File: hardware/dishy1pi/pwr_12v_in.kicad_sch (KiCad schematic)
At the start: 5 parts, among them SW2 SS-12F49-G050, U13 TPS561201DDCR, U14 CYA0630-10UH

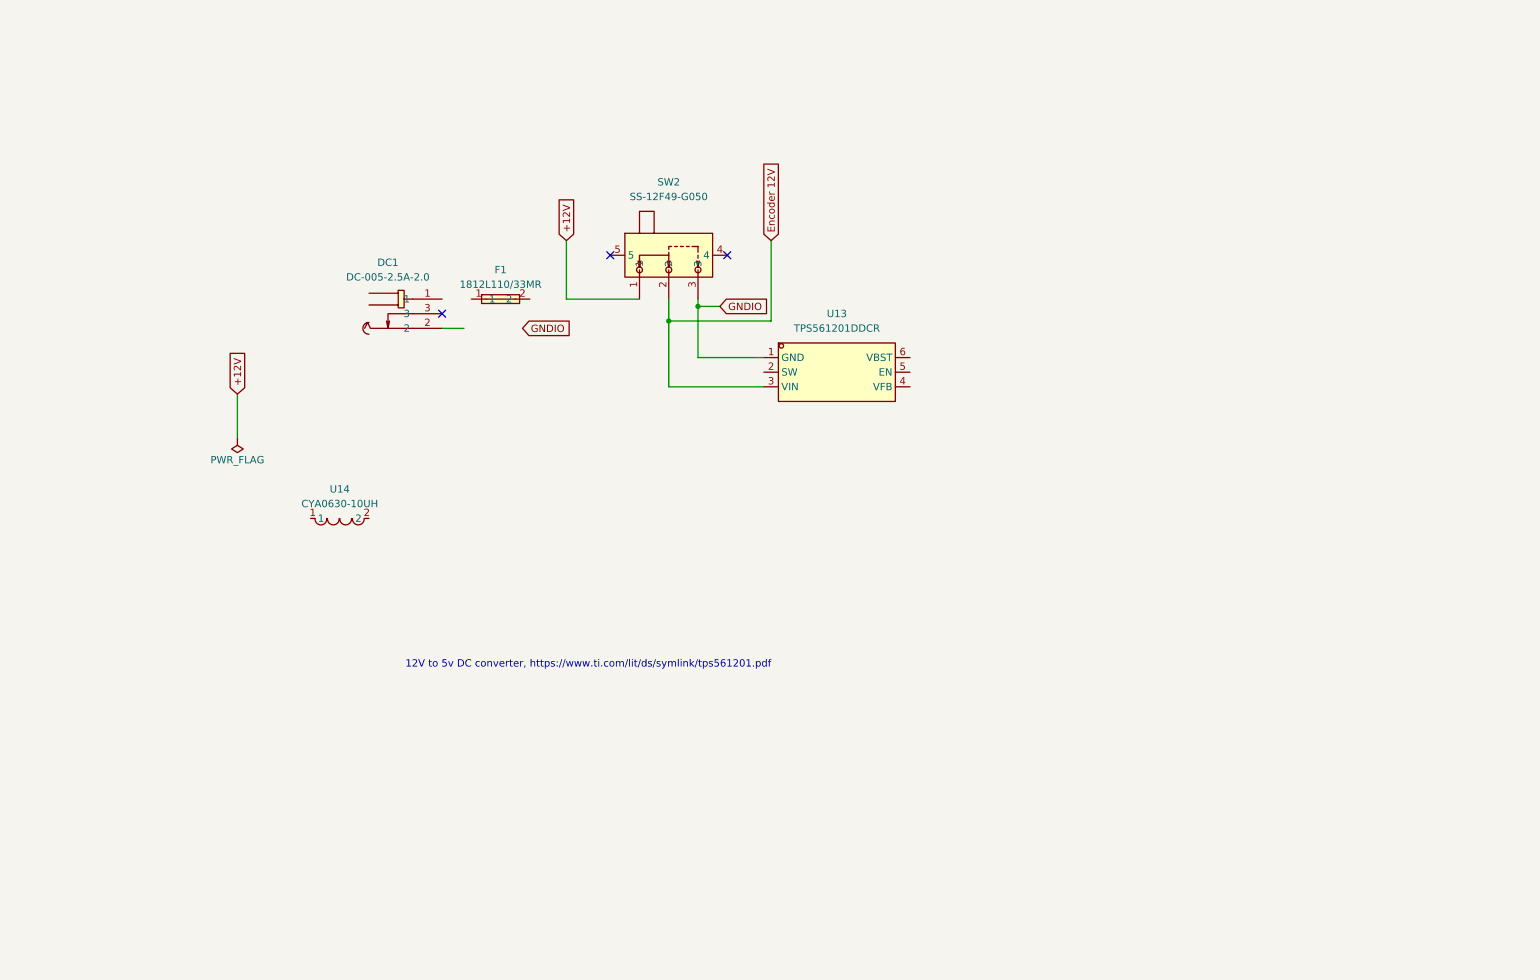
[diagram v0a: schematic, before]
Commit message: Added power circuit to dishy schematic
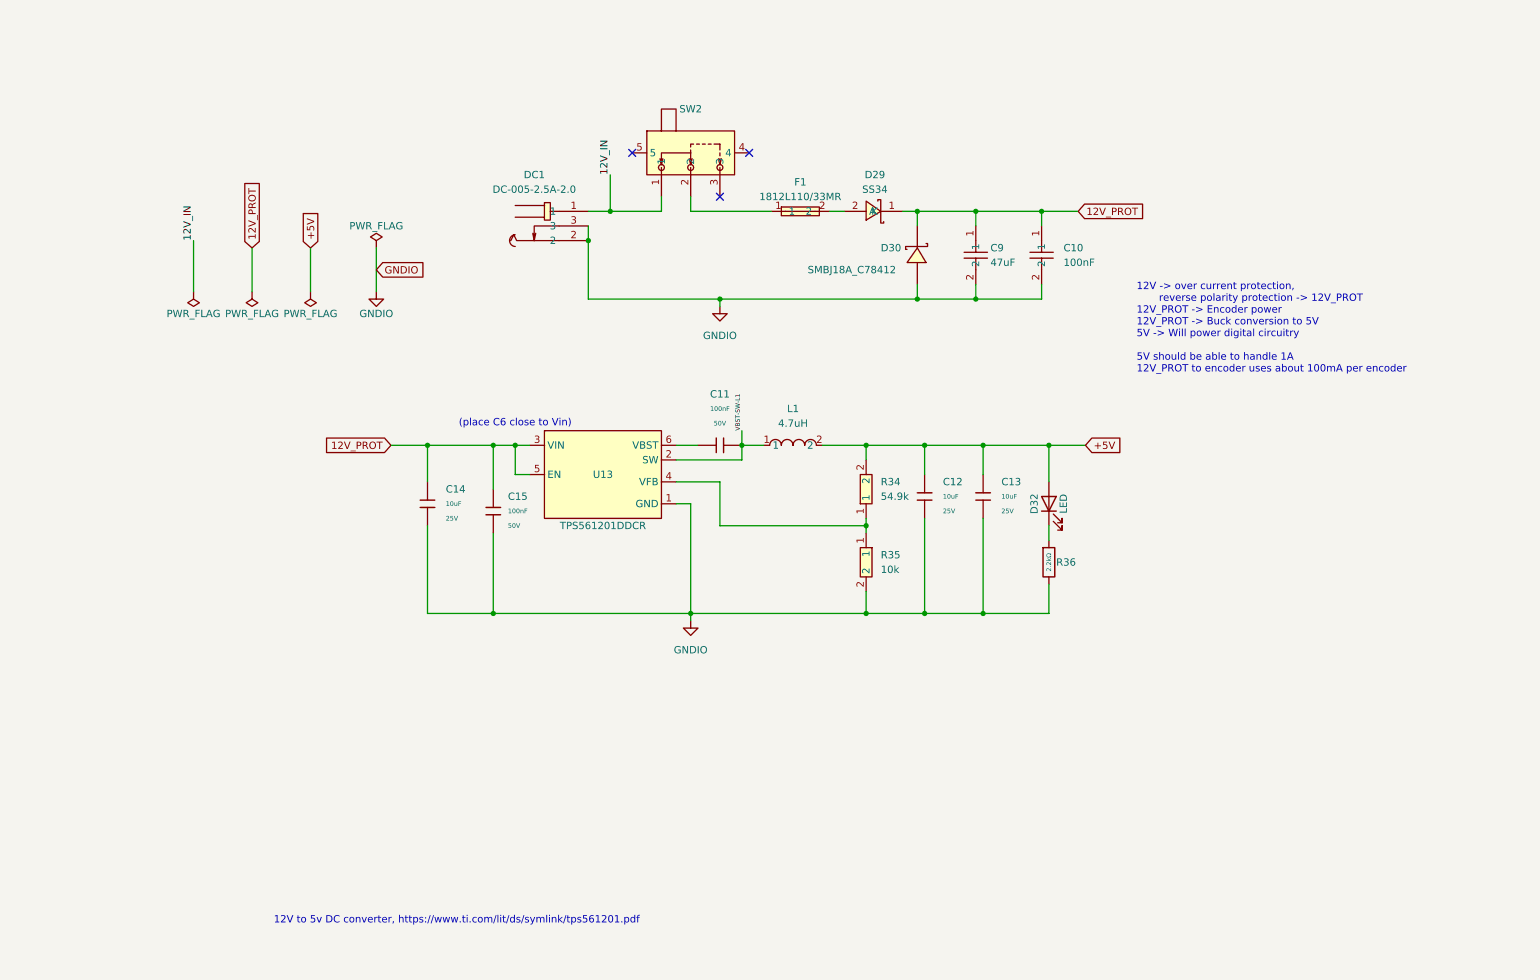
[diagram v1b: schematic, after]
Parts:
- removed DC1: DC-005-2.5A-2.0, MyParts:CONN-TH_DC-005-2.5A-2.0, symbol MyParts:DC-005-2.5A-2.0
- removed F1: 1812L110/33MR, MyParts:F1812, symbol MyParts:1812L110_33MR
- removed SW2: SS-12F49-G050, MyParts:SW-TH_SS-12F45-GXXX, symbol MyParts:SS-12F49-G050
- removed U13: TPS561201DDCR, MyParts:SOT-23-6_L2.9-W1.6-P0.95-LS2.8-BR, symbol MyParts:TPS561201DDCR
- removed U14: CYA0630-10UH, MyParts:IND-SMD_L7.2-W6.6_GPSR07X0, symbol MyParts:CYA0630-10UH
- added C10: 100nF, PowerSupply:C0603, symbol PowerSupply:CC0603KRX7R9BB104
- added C11: 100nF, PCM_JLCPCB:C_0402, symbol PCM_JLCPCB-Capacitors:0402,100nF,(2)
- added C12, C13, C14: 10uF, PCM_JLCPCB:C_0805, symbol PCM_JLCPCB-Capacitors:0805,10uF
- added C15: 100nF, PCM_JLCPCB:C_0805, symbol PCM_JLCPCB-Capacitors:0805,100nF,(2)
- added C9: 47uF, PowerSupply:C1206, symbol PowerSupply:GRM31CR61E476ME44L
- added D29: SS34, PowerSupply:SMA_L4.3-W2.6-LS5.2-RD, symbol PowerSupply:SS34_C8678
- added D30: SMBJ18A_C78412, MyParts:SMB_L4.6-W3.6-LS5.3-RD, symbol PowerSupply:SMBJ18A_C78412
- added D32: LED, LED_SMD:LED_1206_3216Metric, symbol Device:LED
- added DC1: DC-005-2.5A-2.0, PowerSupply:CONN-TH_DC-005-2.5A-2.0, symbol PowerSupply:DC-005-2.5A-2.0
- added F1: 1812L110/33MR, PowerSupply:F1812, symbol PowerSupply:1812L110_33MR
- added L1: 4.7uH, PowerSupply:IND-SMD_L3.0-W3.0-1, symbol PowerSupply:ANR3015T4R7M
- added R34: 54.9k, PowerSupply:R0603, symbol PowerSupply:0603WAF5492T5E
- added R35: 10k, PowerSupply:R0603, symbol PowerSupply:0603WAF1002T5E
- added R36: 2.2kΩ, PCM_JLCPCB:R_0402, symbol PCM_JLCPCB-Resistors:0402,2.2kΩ
- added SW2: SS-12F49-G050, PowerSupply:SW-TH_SS-12F45-GXXX, symbol PowerSupply:SS-12F49-G050
- added U13: TPS561201DDCR, PowerSupply:SOT-23-6_L2.9-W1.6-P0.95-LS2.8-BR, symbol PowerSupply:TPS561201DDCR
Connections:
- net GNDIO: now also C10.2, C12.2, C13.2, C14.2, C15.2, C9.2, D30.2 (A), DC1.2, DC1.3, R35.2, R36.2, U13.1 (GND)
- new net: R34.1, R35.1, U13.4 (VFB)
- new net: C11.1, U13.6 (VBST)
- new net: D32.1 (K), R36.1
- new net: D29.2 (A), F1.2
- new net: F1.1, SW2.2
- new net +5V: C12.1, C13.1, D32.2 (A), L1.2, R34.2
- new net 12V_IN: DC1.1, SW2.1
- new net 12V_PROT: C10.1, C14.1, C15.1, C9.1, D29.1 (K), D30.1 (K), U13.3 (VIN), U13.5 (EN)
- new net VBST-SW-L1: C11.2, L1.1, U13.2 (SW)
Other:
- note added: "(place C6 close to Vin)"
- note added: "12V -> over current protection, reverse polarity protection -> 12V_PROT 12V_PROT -> Encoder power 12V_PROT -> Buck conversion to 5V 5V -> Will power digital circuitry 5V should be able to handle 1A 12V_PROT to encoder uses about 100mA per encoder"

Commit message: Added 12V power input
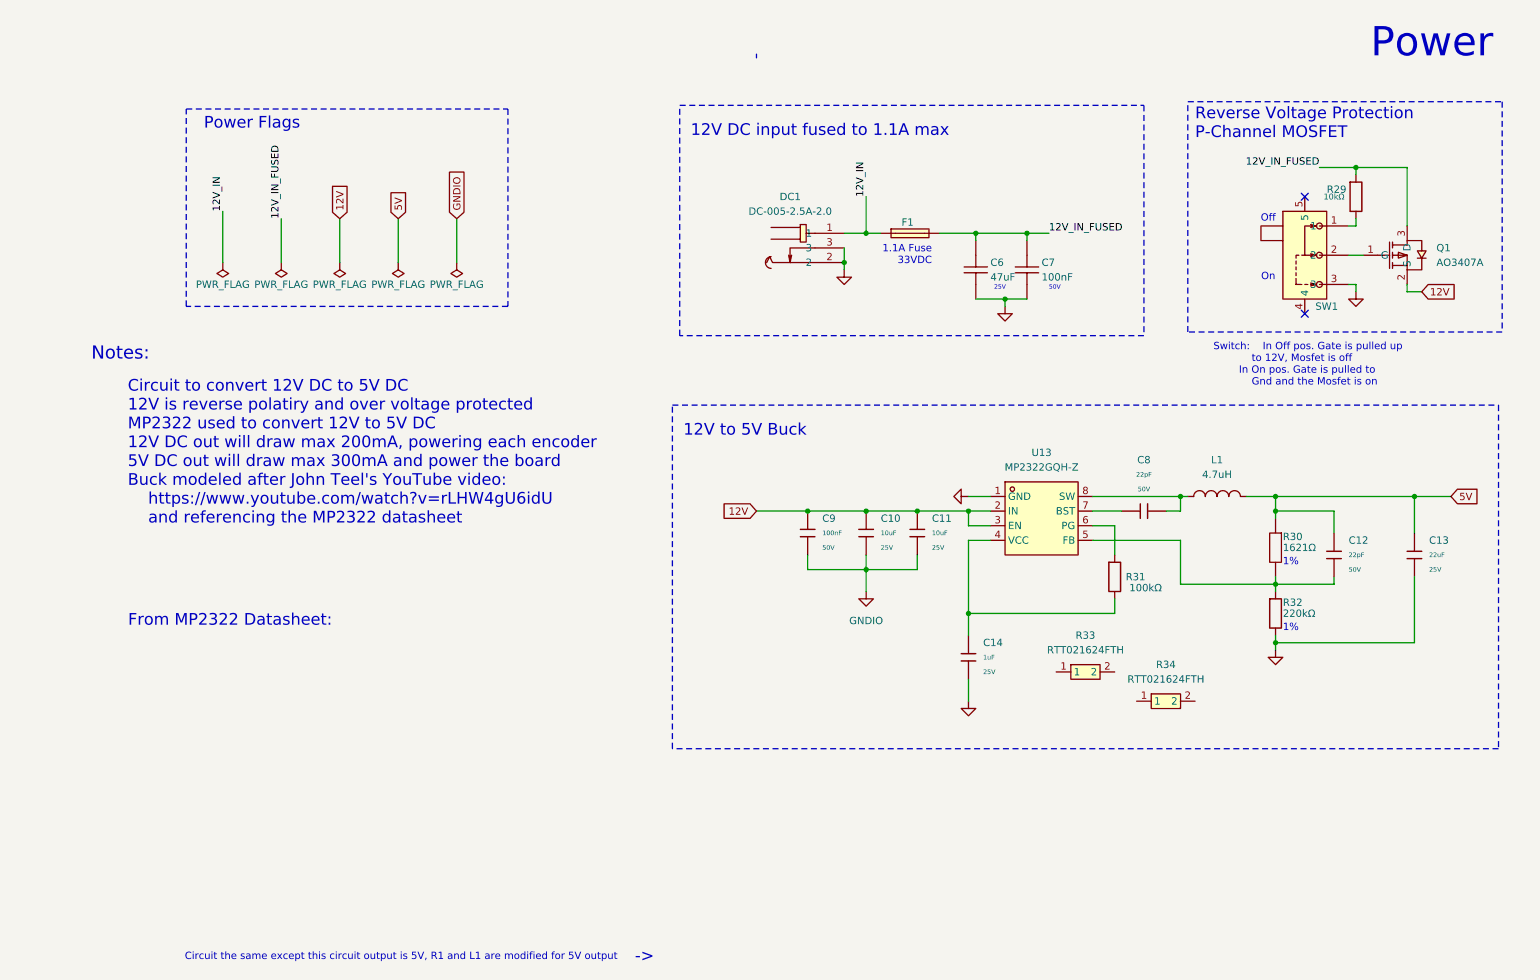
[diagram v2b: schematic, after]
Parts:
- removed C10: 100nF, PowerSupply:C0603, symbol PowerSupply:CC0603KRX7R9BB104
- removed C11: 100nF, PCM_JLCPCB:C_0402, symbol PCM_JLCPCB-Capacitors:0402,100nF,(2)
- removed C12, C13, C14: 10uF, PCM_JLCPCB:C_0805, symbol PCM_JLCPCB-Capacitors:0805,10uF
- removed C15: 100nF, PCM_JLCPCB:C_0805, symbol PCM_JLCPCB-Capacitors:0805,100nF,(2)
- removed C9: 47uF, PowerSupply:C1206, symbol PowerSupply:GRM31CR61E476ME44L
- removed D29: SS34, PowerSupply:SMA_L4.3-W2.6-LS5.2-RD, symbol PowerSupply:SS34_C8678
- removed D30: SMBJ18A_C78412, MyParts:SMB_L4.6-W3.6-LS5.3-RD, symbol PowerSupply:SMBJ18A_C78412
- removed D32: LED, LED_SMD:LED_1206_3216Metric, symbol Device:LED
- removed R34: 54.9k, PowerSupply:R0603, symbol PowerSupply:0603WAF5492T5E
- removed R35: 10k, PowerSupply:R0603, symbol PowerSupply:0603WAF1002T5E
- removed R36: 2.2kΩ, PCM_JLCPCB:R_0402, symbol PCM_JLCPCB-Resistors:0402,2.2kΩ
- removed SW2: SS-12F49-G050, PowerSupply:SW-TH_SS-12F45-GXXX, symbol PowerSupply:SS-12F49-G050
- removed U13: TPS561201DDCR, PowerSupply:SOT-23-6_L2.9-W1.6-P0.95-LS2.8-BR, symbol PowerSupply:TPS561201DDCR
- added C10, C11: 10uF, PCM_JLCPCB:C_0603, symbol PCM_JLCPCB-Capacitors:0603,10uF,(2)
- added C12: 22pF, PCM_JLCPCB:C_0603, symbol PCM_JLCPCB-Capacitors:0603,22pF
- added C13: 22uF, PCM_JLCPCB:C_0805, symbol PCM_JLCPCB-Capacitors:0805,22uF
- added C14: 1uF, PCM_JLCPCB:C_0402, symbol PCM_JLCPCB-Capacitors:0402,1uF
- added C6: 47uF, PowerSupply:C1206, symbol PowerSupply:GRM31CR61E476ME44L
- added C7: 100nF, PowerSupply:C0603, symbol PowerSupply:CC0603KRX7R9BB104
- added C8: 22pF, PCM_JLCPCB:C_0402, symbol PCM_JLCPCB-Capacitors:0402,22pF
- added C9: 100nF, PCM_JLCPCB:C_0603, symbol PCM_JLCPCB-Capacitors:0603,100nF
- added Q1: AO3407A, PowerSupply:SOT-23-3_L2.9-W1.6-P1.90-LS2.8-BR, symbol PowerSupply:AO3407A
- added R29: 10kΩ, PCM_JLCPCB:R_0603, symbol PCM_JLCPCB-Resistors:0603,10kΩ
- added R30: 1621Ω, PowerSupply:R0603, symbol PowerSupply:0603WAF1621T5E
- added R31: 100kΩ, PCM_JLCPCB:R_0603, symbol PCM_JLCPCB-Resistors:0603,100kΩ
- added R32: 220kΩ, PCM_JLCPCB:R_0603, symbol PCM_JLCPCB-Resistors:0603,220kΩ
- added R33, R34: RTT021624FTH, myparts:R0402, symbol MyParts:RTT021624FTH
- added SW1: SS-12F49-G050, PowerSupply:SW-TH_SS-12F45-GXXX, symbol PowerSupply:SS-12F49-G050
- added U13: MP2322GQH-Z, PowerSupply:QFN-8_L2.0-W1.5-P0.50-BL, symbol PowerSupply:MP2322GQH-Z
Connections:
- net 12V_IN: now also F1.1
- net GNDIO: now also C10.2, C11.2, C13.2, C14.2, C6.2, C7.2, C9.2, R32.2, SW1.3, U13.1 (GND)
- net 12V_IN_FUSED: now reaches F1.2
- net 12V_IN_FUSED: now also C6.1, C7.1, Q1.3 (D), R29.1
- net +5V renamed 5V
- net 5V: now also C12.1, C13.1, R30.1
- net VBST-SW-L1: no longer names the net of L1.1
- net VBST-SW-L1: now also C8.2, U13.8 (SW)
- new net: Q1.1 (G), SW1.2
- new net: C12.2, R30.2, R32.1, U13.5 (FB)
- new net: R31.1, U13.6 (PG)
- new net: C14.1, R31.2, U13.4 (VCC)
- new net: C8.1, U13.7 (BST)
- new net: R29.2, SW1.1
- new net 12V: C10.1, C11.1, C9.1, Q1.2 (S), U13.2 (IN), U13.3 (EN)
- no-connect marks 3 -> 2
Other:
- note added: "->"
- note added: "1%"
- note added: "1.1A Fuse 33VDC"
- note added: "12V DC input fused to 1.1A max"
- note added: "12V to 5V Buck"
- note added: "25V"
- note added: "50V"
- note added: "Circuit the same except this circuit output is 5V, R1 and L1 are modified for 5V output"
- note added: "Circuit to convert 12V DC to 5V DC 12V is reverse polatiry and over voltage protected MP2322 used to convert 12V to 5V DC 12V DC out will draw max 200mA, powering each encoder 5V DC out will draw max 300mA and power the board Buck modeled after John Teel's YouTube video: https://www.youtube.com/watch?v=rLHW4gU6idU and referencing the MP2322 datasheet"
- note added: "From MP2322 Datasheet:"
- note added: "Notes:"
- note added: "Off"
- note added: "On"
- note added: "Power"
- note added: "Power Flags"
- note added: "Reverse Voltage Protection P-Channel MOSFET"
- note added: "Switch: In Off pos. Gate is pulled up to 12V, Mosfet is off In On pos. Gate is pulled to Gnd and the Mosfet is on"
- note removed: "(place C6 close to Vin)"
- note removed: "12V -> over current protection, reverse polarity protection -> 12V_PROT 12V_PROT -> Encoder power 12V_PROT -> Buck conversion to 5V 5V -> Will power digital circuitry 5V should be able to handle 1A 12V_PROT to encoder uses about 100mA per encoder"
- note removed: "12V to 5v DC converter, https://www.ti.com/lit/ds/symlink/tps561201.pdf"
- company: (none) -> JRDish
- moved on the sheet: DC1

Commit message: Little change
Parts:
- removed R30: 1621Ω, PowerSupply:R0603, symbol PowerSupply:0603WAF1621T5E
- removed R33, R34: RTT021624FTH, myparts:R0402, symbol MyParts:RTT021624FTH
- added R30: 1624k, MyParts:R0603, symbol MyParts:RS-03L1624FT
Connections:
- net at R32.1, U13.5 (FB): now also R30.1; no longer C12.2
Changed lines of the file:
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@@
 	(text "1%"
 		(exclude_from_sim no)
-		(at 224.79 113.03 0)
+		(at 224.79 114.3 0)
 		(effects
 			(font
@@
 	)
 	(junction
+		(at 223.52 115.57)
+		(diameter 0)
+		(color 0 0 0 0)
+	)
+	(junction
 		(at 223.52 104.14)
 		(diameter 0)
@@
 	(wire
 		(pts
-			(xy 233.68 116.84) (xy 223.52 116.84)
+			(xy 232.41 115.57) (xy 223.52 115.57)
 		)
 		(stroke
@@
 	(wire
 		(pts
+			(xy 223.52 115.57) (xy 222.25 115.57)
+		)
+		(stroke
+			(width 0)
+			(type default)
+		)
+	)
+	(wire
+		(pts
 			(xy 236.22 64.77) (xy 237.49 64.77)
 		)
@@
 	)
 	(symbol
+		(lib_id "MyParts:RS-03L1624FT")
+		(at 223.52 111.76 90)
+		(unit 1)
+		(exclude_from_sim no)
+		(in_bom yes)
+		(on_board yes)
+		(dnp no)
+		(property "Reference" "R30"
+			(at 224.79 109.2199 90)
+			(effects
+				(font
+					(size 1.27 1.27)
+				)
+				(justify right)
+			)
+		)
+		(property "Value" "1624k"
+			(at 224.79 111.7599 90)
+			(effects
+				(font
+					(size 1.27 1.27)
+				)
+				(justify right)
+			)
+		)
+		(property "Footprint" "MyParts:R0603"
+			(at 231.14 111.76 0)
+			(effects
+				(font
+					(size 1.27 1.27)
+				)
+				(hide yes)
+			)
+		)
+		(property "Datasheet" "https://lcsc.com/product-detail/Others_Guangdong-Fenghua-Advanced-Tech-RS-03L1624FT_C322061.html"
+			(at 233.68 111.76 0)
+			(effects
+				(font
+					(size 1.27 1.27)
+				)
+				(hide yes)
+			)
+		)
+		(property "Description" ""
+			(at 223.52 111.76 0)
+			(effects
+				(font
+					(size 1.27 1.27)
+				)
+				(hide yes)
+			)
+		)
+		(property "LCSC Part" "C322061"
+			(at 236.22 111.76 0)
+			(effects
+				(font
+					(size 1.27 1.27)
+				)
+				(hide yes)
+			)
+		)
+		(pin "2"
+		)
+		(pin "1"
+		)
+		(instances
+			(project ""
+				(path "/e63e39d7-6ac0-4ffd-8aa3-1841a4541b55/38a6bbeb-d8bb-40a0-bcd1-f27437131055"
+					(reference "R30")
+					(unit 1)
+				)
+			)
+		)
+	)
+	(symbol
 		(lib_id "power:PWR_FLAG")
 		(at 50.8 60.96 180)
@@
 	)
 	(symbol
-		(lib_id "MyParts:RTT021624FTH")
-		(at 204.47 137.16 0)
-		(unit 1)
-		(exclude_from_sim no)
-		(in_bom yes)
-		(on_board yes)
-		(dnp no)
-		(fields_autoplaced yes)
-		(property "Reference" "R34"
-			(at 204.47 130.81 0)
-			(effects
-				(font
-					(size 1.27 1.27)
-				)
-			)
-		)
-		(property "Value" "RTT021624FTH"
-			(at 204.47 133.35 0)
-			(effects
-				(font
-					(size 1.27 1.27)
-				)
-			)
-		)
-		(property "Footprint" "myparts:R0402"
-			(at 204.47 144.78 0)
-			(effects
-				(font
-					(size 1.27 1.27)
-				)
-				(hide yes)
-			)
-		)
-		(property "Datasheet" "https://lcsc.com/product-detail/Chip-Resistor-Surface-Mount_RALEC-RTT021624FTH_C166525.html"
-			(at 204.47 147.32 0)
-			(effects
-				(font
-					(size 1.27 1.27)
-				)
-				(hide yes)
-			)
-		)
-		(property "Description" ""
-			(at 204.47 137.16 0)
-			(effects
-				(font
-					(size 1.27 1.27)
-				)
-				(hide yes)
-			)
-		)
-		(property "LCSC Part" "C166525"
-			(at 204.47 149.86 0)
-			(effects
-				(font
-					(size 1.27 1.27)
-				)
-				(hide yes)
-			)
-		)
-		(pin "2"
-		)
-		(pin "1"
-		)
-		(instances
-			(project ""
-				(path "/e63e39d7-6ac0-4ffd-8aa3-1841a4541b55/38a6bbeb-d8bb-40a0-bcd1-f27437131055"
-					(reference "R34")
-					(unit 1)
-				)
-			)
-		)
-	)
-	(symbol
 		(lib_id "power:PWR_FLAG")
 		(at 71.12 60.96 180)
@@
 	)
 	(symbol
-		(lib_id "MyParts:RTT021624FTH")
-		(at 190.5 132.08 0)
-		(unit 1)
-		(exclude_from_sim no)
-		(in_bom yes)
-		(on_board yes)
-		(dnp no)
-		(fields_autoplaced yes)
-		(property "Reference" "R33"
-			(at 190.5 125.73 0)
-			(effects
-				(font
-					(size 1.27 1.27)
-				)
-			)
-		)
-		(property "Value" "RTT021624FTH"
-			(at 190.5 128.27 0)
-			(effects
-				(font
-					(size 1.27 1.27)
-				)
-			)
-		)
-		(property "Footprint" "myparts:R0402"
-			(at 190.5 139.7 0)
-			(effects
-				(font
-					(size 1.27 1.27)
-				)
-				(hide yes)
-			)
-		)
-		(property "Datasheet" "https://lcsc.com/product-detail/Chip-Resistor-Surface-Mount_RALEC-RTT021624FTH_C166525.html"
-			(at 190.5 142.24 0)
-			(effects
-				(font
-					(size 1.27 1.27)
-				)
-				(hide yes)
-			)
-		)
-		(property "Description" ""
-			(at 190.5 132.08 0)
-			(effects
-				(font
-					(size 1.27 1.27)
-				)
-				(hide yes)
-			)
-		)
-		(property "LCSC Part" "C166525"
-			(at 190.5 144.78 0)
-			(effects
-				(font
-					(size 1.27 1.27)
-				)
-				(hide yes)
-			)
-		)
-		(pin "1"
-		)
-		(pin "2"
-		)
-		(instances
-			(project ""
-				(path "/e63e39d7-6ac0-4ffd-8aa3-1841a4541b55/38a6bbeb-d8bb-40a0-bcd1-f27437131055"
-					(reference "R33")
-					(unit 1)
-				)
-			)
-		)
-	)
-	(symbol
 		(lib_id "PCM_JLCPCB-Capacitors:0603,22pF")
 		(at 233.68 111.76 0)
@@
 					(unit 1)
 				)
-			)
-		)
-	)
-	(symbol
-		(lib_id "PowerSupply:0603WAF1621T5E")
-		(at 223.52 110.49 270)
-		(unit 1)
-		(exclude_from_sim no)
-		(in_bom yes)
-		(on_board yes)
-		(dnp no)
-		(property "Reference" "R30"
-			(at 224.79 108.585 90)
-			(effects
-				(font
-					(size 1.27 1.27)
-				)
-				(justify left)
-			)
-		)
-		(property "Value" "1621Ω"
-			(at 224.79 110.49 90)
-			(effects
-				(font
-					(size 1.27 1.27)
-				)
-				(justify left)
-			)
-		)
-		(property "Footprint" "PowerSupply:R0603"
-			(at 215.9 110.49 0)
-			(effects
-				(font
-					(size 1.27 1.27)
-				)
-				(hide yes)
-			)
-		)
-		(property "Datasheet" "https://lcsc.com/product-detail/Chip-Resistor-Surface-Mount-UniOhm_1-62KR-1621-1_C22844.html"
-			(at 213.36 110.49 0)
-			(effects
-				(font
-					(size 1.27 1.27)
-				)
-				(hide yes)
-			)
-		)
-		(property "Description" ""
-			(at 223.52 110.49 0)
-			(effects
-				(font
-					(size 1.27 1.27)
-				)
-				(hide yes)
-			)
-		)
-		(property "LCSC Part" "C22844"
-			(at 210.82 110.49 0)
-			(effects
-				(font
-					(size 1.27 1.27)
-				)
-				(hide yes)
-			)
-		)
-		(pin "1"
-		)
-		(pin "2"
-		)
-		(instances
-			(project "DishyPi1"
-				(path "/e63e39d7-6ac0-4ffd-8aa3-1841a4541b55/38a6bbeb-d8bb-40a0-bcd1-f27437131055"
-					(reference "R30")
-					(unit 1)
-				)
